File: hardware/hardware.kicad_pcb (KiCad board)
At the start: 2 copper layers, 14 parts, among them J1 AVR-ISP-6, U2 ATmega88PA-A, U3 CH340C, U4 MPU-6050, U6 AP2112K-3.3, Y1 Crystal

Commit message: up
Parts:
- added G***: LOGO, R-logo:R-logo, F.Cu at (97.5, 40.0)
- added J2: Conn_01x08_MountingPin, Connector_PinHeader_2.54mm:PinHeader_1x08_P2.54mm_Vertical, F.Cu at (87.5, 37.1)
- added J3: Conn_01x08_MountingPin, Connector_PinHeader_2.54mm:PinHeader_1x08_P2.54mm_Vertical, F.Cu at (80.3, 64.7)
- added J4: Conn_01x08_MountingPin, Connector_PinHeader_2.54mm:PinHeader_1x08_P2.54mm_Vertical, F.Cu at (85.0, 64.7)
- Y1: footprint Crystal:Crystal_SMD_HC49-SD -> Crystal:Crystal_SMD_Abracon_ABM7-2Pin_6.0x3.5mm
- moved U6 10.2 mm to (66.1, 59.0)
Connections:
- net RST renamed PC6
- U2 pad 1: unconnected-(U2-PD3-Pad1) -> PD3
- U2 pad 10: unconnected-(U2-PD6-Pad10) -> PD6
- U2 pad 11: unconnected-(U2-PD7-Pad11) -> PD7
- U2 pad 12: PWM -> PB0
- U2 pad 13: AL -> PB1
- U2 pad 14: BL -> PB2
- U2 pad 2: unconnected-(U2-PD4-Pad2) -> PD4
- U2 pad 23: A0 -> PC0
- U2 pad 24: A1 -> PC1
- U2 pad 25: A2 -> PC2
- U2 pad 26: unconnected-(U2-PC3-Pad26) -> PC3
- U2 pad 27: unconnected-(U2-PC4-Pad27) -> PC4
- U2 pad 28: unconnected-(U2-PC5-Pad28) -> PC5
- U2 pad 30: unconnected-(U2-PD0-Pad30) -> PD0
- U2 pad 31: unconnected-(U2-PD1-Pad31) -> PD1
- U2 pad 32: unconnected-(U2-PD2-Pad32) -> MPU_IRQ
- U2 pad 9: unconnected-(U2-PD5-Pad9) -> PD5

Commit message: up
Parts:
- added C10: C, Capacitor_SMD:C_0603_1608Metric, F.Cu at (56.1, 67.4)
- added C11: C, Capacitor_SMD:C_0603_1608Metric, F.Cu at (56.1, 69.9)
- added C12: 1u, Capacitor_SMD:C_0603_1608Metric, F.Cu at (56.1, 72.4)
- added C13: 1u, Capacitor_SMD:C_0603_1608Metric, F.Cu at (66.7, 70.0)
- added C2: C, Capacitor_SMD:C_0603_1608Metric, F.Cu at (56.1, 64.9)
- added D1: LED, Diode_SMD:D_0603_1608Metric, F.Cu at (66.7, 82.4)
- added D2: LED, Diode_SMD:D_0603_1608Metric, F.Cu at (66.7, 85.0)
- added R1: 10k, Resistor_SMD:R_0603_1608Metric, F.Cu at (56.1, 74.9)
- added R2: 10k, Resistor_SMD:R_0603_1608Metric, F.Cu at (56.1, 77.4)
- added R3: 4.7k, Resistor_SMD:R_0603_1608Metric, F.Cu at (56.1, 79.9)
- added R4: 4.7k, Resistor_SMD:R_0603_1608Metric, F.Cu at (56.1, 82.4)
- added R5: 10k, Resistor_SMD:R_0603_1608Metric, F.Cu at (56.1, 84.9)
- added R6: 10k, Resistor_SMD:R_0603_1608Metric, F.Cu at (66.7, 72.5)
- added SW1: SW_Push, Button_Switch_SMD:SW_Push_SPST_NO_Alps_SKRK, F.Cu at (61.4, 83.3)
- added SW2: SW_Push, Button_Switch_SMD:SW_Push_SPST_NO_Alps_SKRK, F.Cu at (67.9, 66.5)
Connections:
- U2 pad 20: unconnected-(U2-AREF-Pad20) -> +5V
- U4 pad 23: SCL -> PC5
- U4 pad 24: SDA -> PC4

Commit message: finish wiring
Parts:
- added J5: USB_B_Micro, Connector_USB:USB_Micro-B_GCT_USB3076-30-A, F.Cu at (74.0, 89.2)
- Y1: footprint Crystal:Crystal_SMD_Abracon_ABM7-2Pin_6.0x3.5mm -> Crystal:Crystal_SMD_2012-2Pin_2.0x1.2mm
- moved C1 41.8 mm to (84.0, 75.0), turned to 180 degrees
- moved C6 38.9 mm to (84.0, 81.5)
- moved U3 37.9 mm to (74.7, 82.3), turned to -90 degrees
- moved C5 36.9 mm to (84.0, 76.5), turned to 180 degrees
- moved U2 28.4 mm to (68.5, 73.0), turned to -90 degrees
- moved J4 28.3 mm to (57.0, 68.7)
- moved R1 27.9 mm to (81.5, 86.5), turned to -90 degrees
- moved SW2 27.5 mm to (84.5, 88.4), turned to 90 degrees
- moved C9 27.3 mm to (85.5, 69.8), turned to -90 degrees
- moved U6 26.8 mm to (84.0, 79.0)
- moved C3 25.3 mm to (69.0, 66.5)
- moved G*** 25.2 mm to (88.2, 63.4)
- moved C8 24.9 mm to (78.4, 73.0), turned to 90 degrees
- moved C7 24.5 mm to (78.4, 69.8), turned to -90 degrees
- moved U4 23.4 mm to (81.9, 71.0)
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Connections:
- C13 pad 1: Net-(C13-Pad1) -> PB0
- C5 pad 1: +3V3 -> +5V
- J4 pad 7: unconnected-(J4-Pin_7-Pad7) -> +3V3
- R5 pad 1: +3.3V -> +5V
- R6 pad 1: +3.3V -> +5V
- R6 pad 2: Net-(C13-Pad1) -> PB0
- SW2 pad 2: Net-(C13-Pad1) -> PB0
- U3 pad 16: +3V3 -> +5V
- U3 pad 2: TX-PROG -> PD0
- U3 pad 3: RX-PROG -> PD1
- U3 pad 4: +3V3 -> unconnected-(U3-V3-Pad4)
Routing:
- net +5V: track 0.00 -> 83.1 mm, vias 0 -> 2
- net +3V3: track 0.00 -> 60.3 mm, vias 0 -> 3
- net PC6: track 0.00 -> 51.1 mm, vias 0 -> 3
- net PB0: track 0.00 -> 46.5 mm, vias 0 -> 2
- net SCK: track 0.00 -> 45.0 mm, vias 0 -> 2
- net PC5: track 0.00 -> 40.9 mm, vias 0 -> 1
- net MPU_IRQ: track 0.00 -> 39.9 mm, vias 0 -> 3
- net PD0: track 0.00 -> 35.1 mm, vias 0 -> 2
- net PD1: track 0.00 -> 33.1 mm, vias 0 -> 2
- net PC4: track 0.00 -> 31.8 mm, vias 0 -> 1
- net PC0: track 0.00 -> 25.4 mm, vias 0 -> 1
- net PC1: track 0.00 -> 23.4 mm, vias 0 -> 1
- net GND: track 0.00 -> 21.8 mm, vias 0 -> 41
- net PC2: track 0.00 -> 19.8 mm, vias 0 -> 1
- net PC3: track 0.00 -> 19.5 mm, vias 0 -> 1
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- added copper zone on B.Cu, net GND
- added copper zone on F.Cu, net GND
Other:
- board outline added: 34 x 33 mm
- board text added: "0/RX 1/TX 2/IN0 3/INT1 4 5 6/AIN0 7/AIN1"
- board text added: "14/A0 15/A1 16/A2 17/A3 18/A4 19/A5 RESET GND"
- board text added: "8 9 10/SS 11/MOSI 12/MISO 13/SCK 3.3 5V"

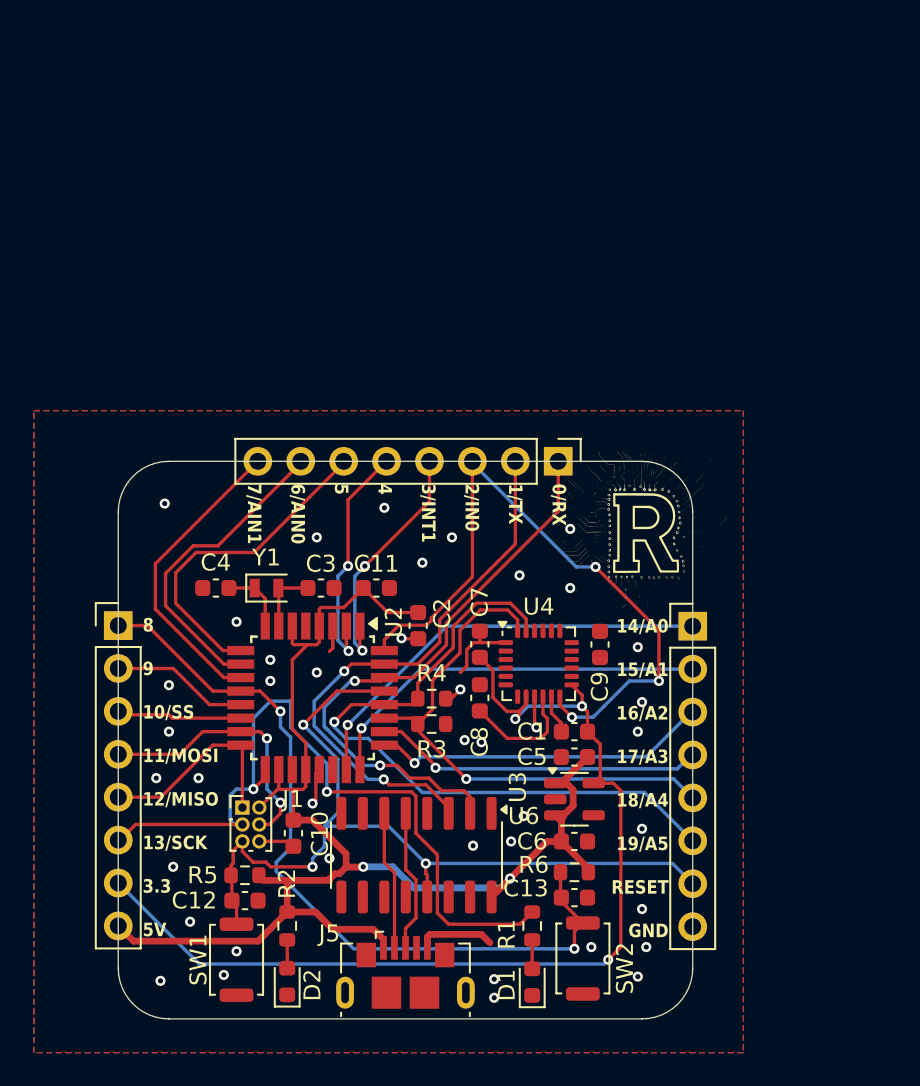
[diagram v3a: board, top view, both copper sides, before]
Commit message: update parts lcsc
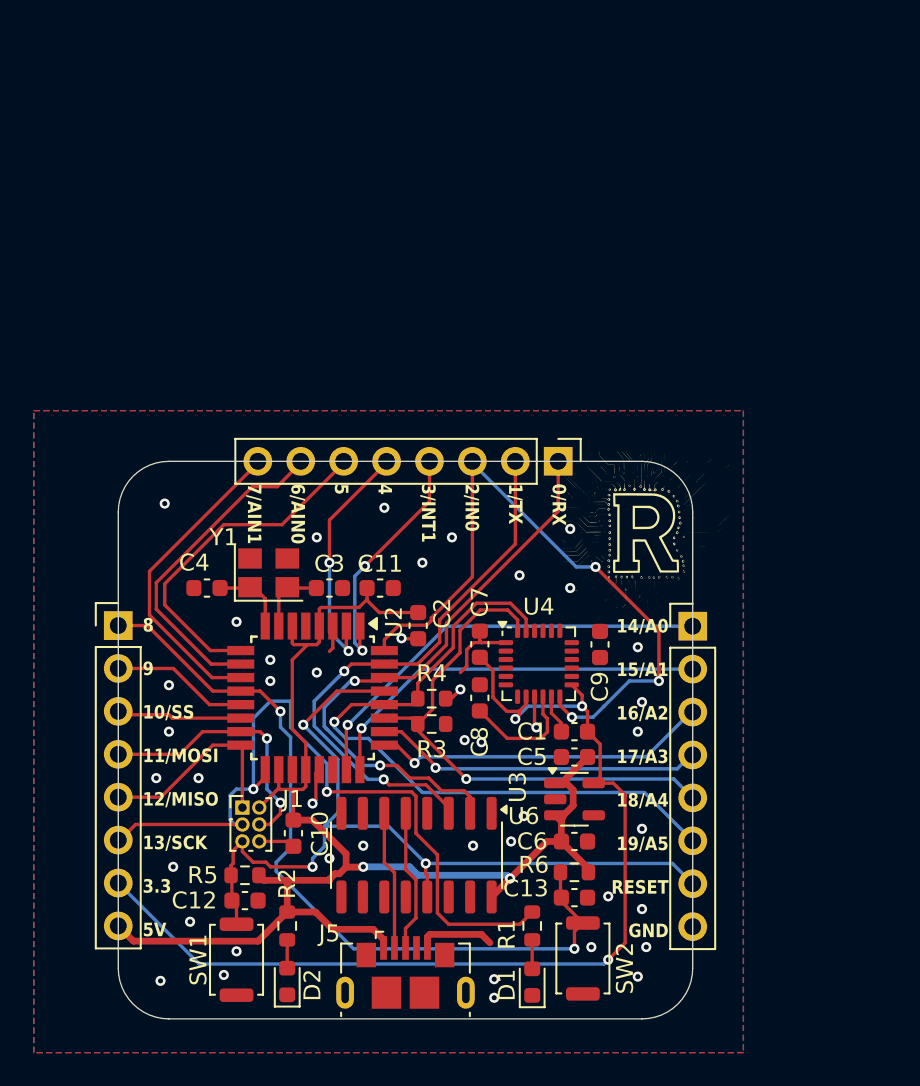
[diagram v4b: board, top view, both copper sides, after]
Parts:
- C12, C13: value 1u -> C
- C3, C4: value 10u -> C
- R1: value 10k -> 2K
- R2: value 10k -> 4.7K
- Y1: footprint Crystal:Crystal_SMD_2012-2Pin_2.0x1.2mm -> Crystal:Crystal_SMD_3225-4Pin_3.2x2.5mm
- moved Y1 0.91 mm to (65.9, 65.6)
- moved C4 0.52 mm to (62.2, 66.5)
- moved C3 0.50 mm to (69.5, 66.5)
- moved C11 0.22 mm to (72.5, 66.5)
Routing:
- net PD5: track 19.4 -> 20.4 mm
- net PD6: track 18.5 -> 19.4 mm
- net PD7: track 17.9 -> 18.6 mm
- net XTAL2: track 4.03 -> 4.56 mm
- net GND: vias 41 -> 43

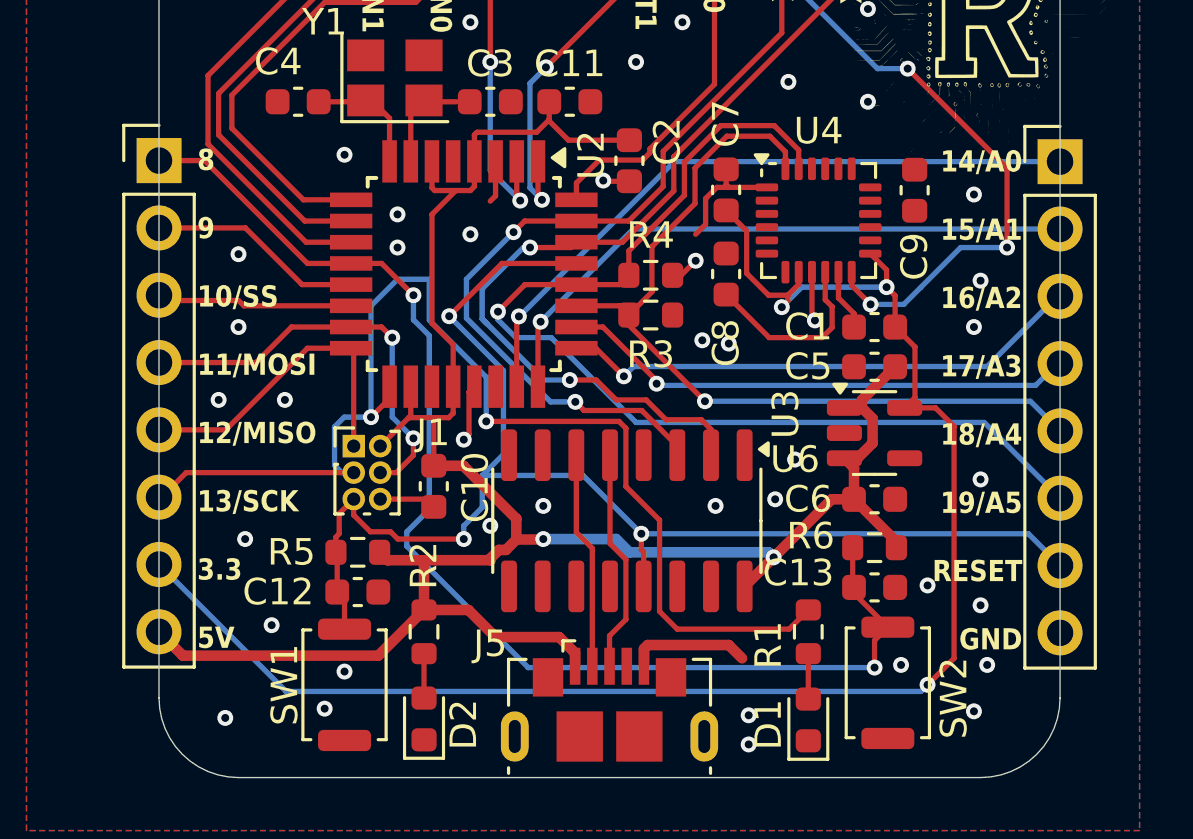
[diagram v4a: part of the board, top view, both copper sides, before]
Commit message: fix user button capacitor ground
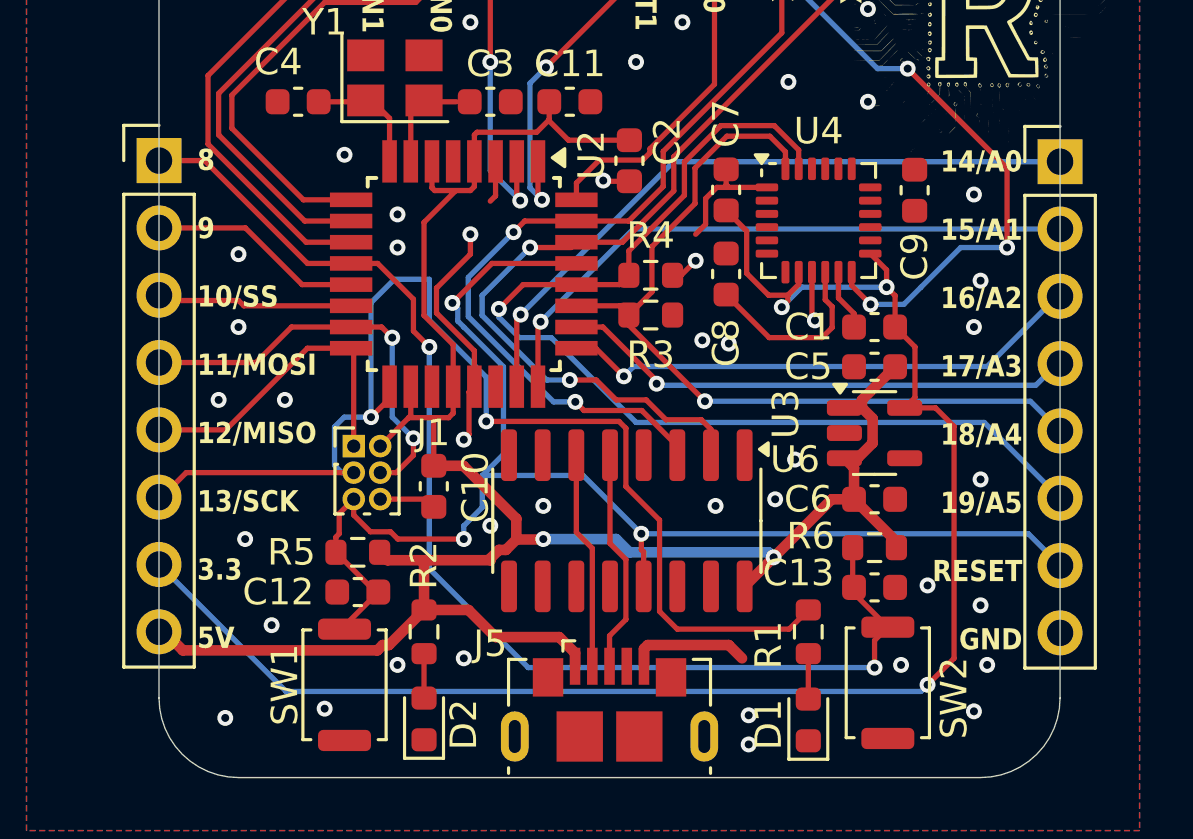
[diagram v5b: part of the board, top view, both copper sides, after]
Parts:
- turned C12 to 180 degrees
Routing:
- net GND: track 21.8 -> 29.0 mm, vias 43 -> 44
- net PC6: track 51.1 -> 52.4 mm
- net PB0: track 46.5 -> 45.7 mm
- net PD0: track 35.1 -> 34.5 mm
